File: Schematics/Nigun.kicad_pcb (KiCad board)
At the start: 4 copper layers, 53.9 x 50.8 mm, 146 parts, among them J1 USB-MICRO-B, J2 RF_INPUT, J3 RF_OUTPUT, P1 CONN_02X04, P2 CONN_SWD, SW1 SW_PUSH_SMALL_H, T1 TC1-1-43A+, T2 TC4-1W+, U2 SKY13351, U3 MIC5504-3.3YM5-TR, U4 AP7365-WG-7, U5 LP0805A0881AS, U6 ADRF6612, U7 FOX924B-16.000, U8 SKY13373, U9 ATSAMD21E

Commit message: Finished PCB editing, first version of gerber files
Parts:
- added M1: Mounting_hole, Footprints:Mounting_hole_100mil, F.Cu at (119.0, 89.8)
- added M2: Mounting_hole, Footprints:Mounting_hole_100mil, F.Cu at (121.9, 49.3)
- added M3: Mounting_hole, Footprints:Mounting_hole_100mil, F.Cu at (166.3, 90.3)
- added M4: Mounting_hole, Footprints:Mounting_hole_100mil, F.Cu at (161.0, 47.0)
- added REF**: Via_10mil, Footprints:Via_drill12mil_pad18mil, F.Cu at (156.3, 78.8)
- added REF**: Via_10mil, Footprints:Via_drill12mil_pad18mil, F.Cu at (142.4, 59.4)
- added REF**: Via_10mil, Footprints:Via_drill12mil_pad18mil, F.Cu at (142.4, 58.1)
- added REF**: Via_10mil, Footprints:Via_drill12mil_pad18mil, F.Cu at (142.4, 56.9)
- added REF**: Via_10mil, Footprints:Via_drill12mil_pad18mil, F.Cu at (142.4, 55.6)
- added REF**: Via_10mil, Footprints:Via_drill12mil_pad18mil, F.Cu at (141.1, 59.4)
- added REF**: Via_10mil, Footprints:Via_drill12mil_pad18mil, F.Cu at (141.1, 58.1)
- added REF**: Via_10mil, Footprints:Via_drill12mil_pad18mil, F.Cu at (141.1, 56.9)
- added REF**: Via_10mil, Footprints:Via_drill12mil_pad18mil, F.Cu at (141.1, 55.6)
- added REF**: Via_10mil, Footprints:Via_drill12mil_pad18mil, F.Cu at (139.9, 59.4)
- added REF**: Via_10mil, Footprints:Via_drill12mil_pad18mil, F.Cu at (139.9, 58.1)
- added REF**: Via_10mil, Footprints:Via_drill12mil_pad18mil, F.Cu at (156.3, 77.5)
- added REF**: Via_10mil, Footprints:Via_drill12mil_pad18mil, F.Cu at (139.9, 56.9)
- added REF**: Via_10mil, Footprints:Via_drill12mil_pad18mil, F.Cu at (139.9, 55.6)
- added REF**: Via_10mil, Footprints:Via_drill12mil_pad18mil, F.Cu at (138.6, 59.4)
- added REF**: Via_10mil, Footprints:Via_drill12mil_pad18mil, F.Cu at (138.6, 58.1)
- added REF**: Via_10mil, Footprints:Via_drill12mil_pad18mil, F.Cu at (138.6, 56.9)
- added REF**: Via_10mil, Footprints:Via_drill12mil_pad18mil, F.Cu at (138.6, 55.6)
- added REF**: Via_10mil, Footprints:Via_drill12mil_pad18mil, F.Cu at (119.0, 53.7)
- added REF**: Via_10mil, Footprints:Via_drill12mil_pad18mil, F.Cu at (120.3, 53.7)
- added REF**: Via_10mil, Footprints:Via_drill12mil_pad18mil, F.Cu at (119.6, 55.2)
- added REF**: Via_10mil, Footprints:Via_drill12mil_pad18mil, F.Cu at (120.9, 55.2)
- added REF**: Via_10mil, Footprints:Via_drill12mil_pad18mil, F.Cu at (156.3, 76.2)
- added REF**: Via_10mil, Footprints:Via_drill12mil_pad18mil, F.Cu at (130.3, 53.2)
- added REF**: Via_10mil, Footprints:Via_drill12mil_pad18mil, F.Cu at (130.8, 54.7)
- added REF**: Via_10mil, Footprints:Via_drill12mil_pad18mil, F.Cu at (130.7, 53.9)
- added REF**: Via_10mil, Footprints:Via_drill12mil_pad18mil, F.Cu at (128.8, 54.2)
- added REF**: Via_10mil, Footprints:Via_drill12mil_pad18mil, F.Cu at (129.2, 54.9)
- added REF**: Via_10mil, Footprints:Via_drill12mil_pad18mil, F.Cu at (128.7, 55.6)
- added REF**: Via_10mil, Footprints:Via_drill12mil_pad18mil, F.Cu at (126.1, 57.1)
- added REF**: Via_10mil, Footprints:Via_drill12mil_pad18mil, F.Cu at (125.1, 57.1)
- added REF**: Via_10mil, Footprints:Via_drill12mil_pad18mil, F.Cu at (124.8, 55.5)
- added REF**: Via_10mil, Footprints:Via_drill12mil_pad18mil, F.Cu at (123.6, 55.7)
- added REF**: Via_10mil, Footprints:Via_drill12mil_pad18mil, F.Cu at (155.0, 78.8)
- added REF**: Via_10mil, Footprints:Via_drill12mil_pad18mil, F.Cu at (124.1, 57.5)
- added REF**: Via_10mil, Footprints:Via_drill12mil_pad18mil, F.Cu at (123.8, 62.4)
- added REF**: Via_10mil, Footprints:Via_drill12mil_pad18mil, F.Cu at (123.8, 61.1)
- added REF**: Via_10mil, Footprints:Via_drill12mil_pad18mil, F.Cu at (123.8, 59.9)
- added REF**: Via_10mil, Footprints:Via_drill12mil_pad18mil, F.Cu at (123.8, 58.6)
- added REF**: Via_10mil, Footprints:Via_drill12mil_pad18mil, F.Cu at (122.2, 57.9)
- added REF**: Via_10mil, Footprints:Via_drill12mil_pad18mil, F.Cu at (122.2, 59.1)
- added REF**: Via_10mil, Footprints:Via_drill12mil_pad18mil, F.Cu at (122.2, 60.4)
- added REF**: Via_10mil, Footprints:Via_drill12mil_pad18mil, F.Cu at (122.2, 61.7)
- added REF**: Via_10mil, Footprints:Via_drill12mil_pad18mil, F.Cu at (122.2, 63.0)
- added REF**: Via_10mil, Footprints:Via_drill12mil_pad18mil, F.Cu at (155.0, 77.5)
- added REF**: Via_10mil, Footprints:Via_drill12mil_pad18mil, F.Cu at (123.7, 69.6)
- added REF**: Via_10mil, Footprints:Via_drill12mil_pad18mil, F.Cu at (123.7, 70.8)
- added REF**: Via_10mil, Footprints:Via_drill12mil_pad18mil, F.Cu at (123.7, 72.1)
- added REF**: Via_10mil, Footprints:Via_drill12mil_pad18mil, F.Cu at (123.7, 73.4)
- added REF**: Via_10mil, Footprints:Via_drill12mil_pad18mil, F.Cu at (123.7, 74.6)
- added REF**: Via_10mil, Footprints:Via_drill12mil_pad18mil, F.Cu at (123.7, 75.9)
- added REF**: Via_10mil, Footprints:Via_drill12mil_pad18mil, F.Cu at (123.7, 68.3)
- added REF**: Via_10mil, Footprints:Via_drill12mil_pad18mil, F.Cu at (122.2, 67.8)
- added REF**: Via_10mil, Footprints:Via_drill12mil_pad18mil, F.Cu at (122.2, 69.1)
- added REF**: Via_10mil, Footprints:Via_drill12mil_pad18mil, F.Cu at (122.2, 70.4)
- added REF**: Via_10mil, Footprints:Via_drill12mil_pad18mil, F.Cu at (155.0, 76.2)
- added REF**: Via_10mil, Footprints:Via_drill12mil_pad18mil, F.Cu at (122.2, 71.6)
- added REF**: Via_10mil, Footprints:Via_drill12mil_pad18mil, F.Cu at (122.2, 72.9)
- added REF**: Via_10mil, Footprints:Via_drill12mil_pad18mil, F.Cu at (122.2, 74.2)
- added REF**: Via_10mil, Footprints:Via_drill12mil_pad18mil, F.Cu at (122.2, 75.5)
- added REF**: Via_10mil, Footprints:Via_drill12mil_pad18mil, F.Cu at (122.2, 76.7)
- added REF**: Via_10mil, Footprints:Via_drill12mil_pad18mil, F.Cu at (122.0, 82.2)
- added REF**: Via_10mil, Footprints:Via_drill12mil_pad18mil, F.Cu at (122.0, 83.5)
- added REF**: Via_10mil, Footprints:Via_drill12mil_pad18mil, F.Cu at (122.0, 84.8)
- added REF**: Via_10mil, Footprints:Via_drill12mil_pad18mil, F.Cu at (122.0, 86.0)
- added REF**: Via_10mil, Footprints:Via_drill12mil_pad18mil, F.Cu at (123.7, 84.1)
- added REF**: Via_10mil, Footprints:Via_drill12mil_pad18mil, F.Cu at (153.8, 78.8)
- added REF**: Via_10mil, Footprints:Via_drill12mil_pad18mil, F.Cu at (123.7, 85.2)
- added REF**: Via_10mil, Footprints:Via_drill12mil_pad18mil, F.Cu at (123.8, 86.5)
- added REF**: Via_10mil, Footprints:Via_drill12mil_pad18mil, F.Cu at (132.5, 87.1)
- added REF**: Via_10mil, Footprints:Via_drill12mil_pad18mil, F.Cu at (131.2, 87.1)
- added REF**: Via_10mil, Footprints:Via_drill12mil_pad18mil, F.Cu at (129.9, 87.1)
- added REF**: Via_10mil, Footprints:Via_drill12mil_pad18mil, F.Cu at (126.1, 87.1)
- added REF**: Via_10mil, Footprints:Via_drill12mil_pad18mil, F.Cu at (124.9, 87.1)
- added REF**: Via_10mil, Footprints:Via_drill12mil_pad18mil, F.Cu at (127.4, 87.1)
- added REF**: Via_10mil, Footprints:Via_drill12mil_pad18mil, F.Cu at (133.7, 87.1)
- added REF**: Via_10mil, Footprints:Via_drill12mil_pad18mil, F.Cu at (135.0, 87.1)
- added REF**: Via_10mil, Footprints:Via_drill12mil_pad18mil, F.Cu at (153.8, 77.5)
- added REF**: Via_10mil, Footprints:Via_drill12mil_pad18mil, F.Cu at (128.7, 87.1)
- added REF**: Via_10mil, Footprints:Via_drill12mil_pad18mil, F.Cu at (141.9, 89.0)
- added REF**: Via_10mil, Footprints:Via_drill12mil_pad18mil, F.Cu at (140.7, 89.0)
- added REF**: Via_10mil, Footprints:Via_drill12mil_pad18mil, F.Cu at (139.4, 89.0)
- added REF**: Via_10mil, Footprints:Via_drill12mil_pad18mil, F.Cu at (138.1, 89.0)
- added REF**: Via_10mil, Footprints:Via_drill12mil_pad18mil, F.Cu at (136.9, 89.0)
- added REF**: Via_10mil, Footprints:Via_drill12mil_pad18mil, F.Cu at (135.6, 89.0)
- added REF**: Via_10mil, Footprints:Via_drill12mil_pad18mil, F.Cu at (134.3, 89.0)
- added REF**: Via_10mil, Footprints:Via_drill12mil_pad18mil, F.Cu at (133.1, 89.0)
- added REF**: Via_10mil, Footprints:Via_drill12mil_pad18mil, F.Cu at (131.8, 89.0)
- added REF**: Via_10mil, Footprints:Via_drill12mil_pad18mil, F.Cu at (153.8, 76.2)
- added REF**: Via_10mil, Footprints:Via_drill12mil_pad18mil, F.Cu at (130.5, 89.0)
- added REF**: Via_10mil, Footprints:Via_drill12mil_pad18mil, F.Cu at (129.2, 89.0)
- added REF**: Via_10mil, Footprints:Via_drill12mil_pad18mil, F.Cu at (128.0, 89.0)
- added REF**: Via_10mil, Footprints:Via_drill12mil_pad18mil, F.Cu at (126.7, 89.0)
- added REF**: Via_10mil, Footprints:Via_drill12mil_pad18mil, F.Cu at (125.4, 89.0)
- moved SW1 51.7 mm to (122.8, 44.9)
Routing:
- net Net-(R32-Pad1): track 2.94 -> 74.5 mm, vias 0 -> 2
- net /VCC_3.7V: track 167.4 -> 187.2 mm
- net Earth: track 121.0 -> 134.5 mm
- net ADRF_CSNOT: track 52.8 -> 50.7 mm
- net Net-(T1-Pad6): track 28.9 -> 27.2 mm
- net IN_SW_VCTL1: track 134.5 -> 135.1 mm
- added copper zone on GND, net Earth
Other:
- rule via_min_size: 0.4 -> 0.254

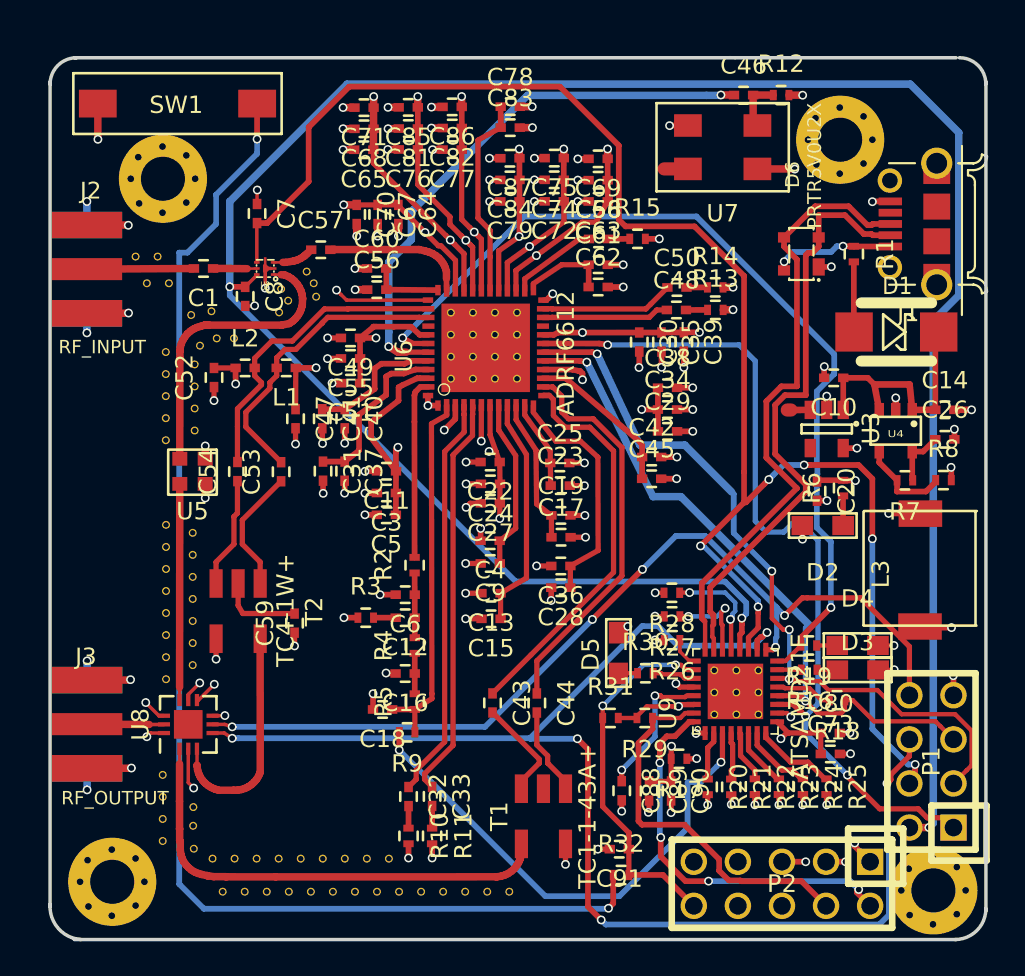
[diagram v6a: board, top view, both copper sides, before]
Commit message: Added 3d model, updated components and readme
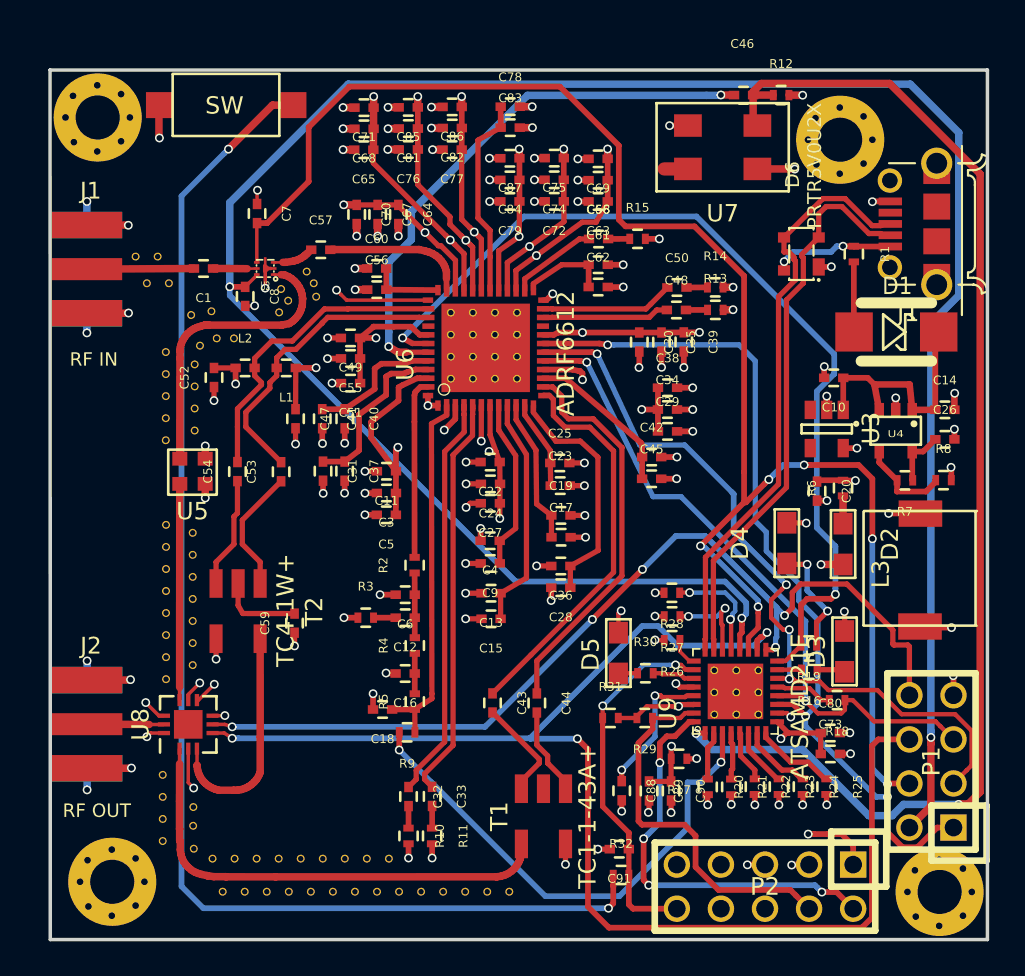
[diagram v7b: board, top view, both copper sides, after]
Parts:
- J1: renamed from J2; value RF_INPUT -> RF IN; footprint adafruit:SMA_EDGELAUNCH -> Footprints:SMA_EDGELAUNCH
- J2: renamed from J3; value RF_OUTPUT -> RF OUT; footprint adafruit:SMA_EDGELAUNCH -> Footprints:SMA_EDGELAUNCH
- U6: footprint ADRF6612_LFCSP48:LFCSP48 -> Footprints:ADRF6612
- moved D4 7.17 mm to (157.9, 70.3), turned to 270 degrees
- moved M2 5.16 mm to (118.2, 45.7)
- moved SW 3.15 mm to (125.9, 45.0)
- moved D2 1.58 mm to (161.1, 70.3), turned to 90 degrees
- moved D3 1.31 mm to (161.2, 76.5), turned to 270 degrees
- moved P2 0.99 mm to (156.6, 90.0)
- moved M3 0.37 mm to (166.7, 90.3)
- renumbered SW1 to SW
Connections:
- REF** pad 1: (no net) -> Earth (x9)
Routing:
- net TCXO_OUT: track 3.58 -> 73.7 mm, vias 1 -> 2
- net Net-(D4-Pad2): track 1.19 -> 6.61 mm, vias 0 -> 2
- net USB_D-: track 34.7 -> 32.7 mm
- net USB_D+: track 35.7 -> 34.1 mm
- net OUT_SW_V2: track 53.9 -> 55.6 mm
- net Net-(U3-Pad3): track 1.32 -> 0.00 mm
- net Earth: track 134.5 -> 135.6 mm
- net Net-(R32-Pad1): track 74.5 -> 75.6 mm
- net SWDIO: track 22.5 -> 23.5 mm
- net ADRF_MUXOUT: track 52.7 -> 53.7 mm
- net ADRF_SCLK: track 43.6 -> 44.4 mm
- net IN_SW_VCTL2: track 94.3 -> 95.0 mm
- net IN_SW_VCTL1: track 135.1 -> 134.4 mm
- net OUT_SW_V1: track 78.1 -> 78.8 mm, vias 5 -> 3
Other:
- board size 53.9 x 50.8 mm -> 54 x 50.1 mm
- net class Differential pair: trace_width 0.3302 -> 0.3048

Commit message: Design update
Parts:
- D6: value PRTR5V0U2X -> ESD PROTECTION
- T1: value TC1-1-43A+ -> TC1
- T2: value TC4-1W+ -> TC4
- moved M2 1.62 mm to (118.4, 47.3)
- renumbered U7 to TCXO
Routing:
- net /VCC_3.7V: track 187.2 -> 202.3 mm, vias 24 -> 25
- net /VCC_3.3V: track 76.5 -> 90.2 mm
- net TCXO_OUT: track 73.7 -> 75.2 mm
- net Net-(U7-Pad1): track 1.37 -> 0.00 mm
- net /MCU_VDDIN: track 47.8 -> 48.3 mm
